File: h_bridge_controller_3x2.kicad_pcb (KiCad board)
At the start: 2 copper layers, 69.8 x 40.6 mm, 1 part

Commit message: Progress towards v1.0.
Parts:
- added C1: 0.1uF, h_bridge_controller_3x2:SM1210, F.Cu at (226.1, 101.3)
- added C2: 0.1uF, h_bridge_controller_3x2:SM1210, F.Cu at (238.4, 91.5)
- added C3: 47uF, h_bridge_controller_3x2:SM2917_POL, F.Cu at (208.5, 105.6)
- added D1: diode_schottky_45V_10A, h_bridge_controller_3x2:CFP15, F.Cu at (175.5, 120.5)
- added D2: diode_schottky_40V_1A, h_bridge_controller_3x2:DO-214AC(SMA), F.Cu at (175.0, 97.2)
- added D3: diode_schottky_40V_1A, h_bridge_controller_3x2:DO-214AC(SMA), F.Cu at (175.0, 103.9)
- added D4: diode_schottky_40V_1A, h_bridge_controller_3x2:DO-214AC(SMA), F.Cu at (209.8, 71.2)
- added D5: diode_schottky_40V_1A, h_bridge_controller_3x2:DO-214AC(SMA), F.Cu at (209.8, 77.9)
- added D6: diode_schottky_40V_1A, h_bridge_controller_3x2:DO-214AC(SMA), F.Cu at (193.1, 97.2)
- added D7: diode_schottky_40V_1A, h_bridge_controller_3x2:DO-214AC(SMA), F.Cu at (193.1, 103.9)
- added D8: diode_schottky_40V_1A, h_bridge_controller_3x2:DO-214AC(SMA), F.Cu at (227.9, 71.2)
- added D9: diode_schottky_40V_1A, h_bridge_controller_3x2:DO-214AC(SMA), F.Cu at (209.8, 84.6)
- added L1: LED_24V, h_bridge_controller_3x2:LED_555-3XXX, F.Cu at (205.8, 95.5)
- added L2: LED_24V, h_bridge_controller_3x2:LED_555-3XXX, F.Cu at (212.8, 95.5)
- added L3: LED_24V, h_bridge_controller_3x2:LED_555-3XXX, F.Cu at (219.9, 98.2)
- added L4: LED_24V, h_bridge_controller_3x2:LED_555-3XXX, F.Cu at (239.3, 82.1)
- added L5: LED_24V, h_bridge_controller_3x2:LED_555-3XXX, F.Cu at (256.4, 75.3)
- added P1: PWR_JACK_2.5x5.5, h_bridge_controller_3x2:DCJACK_2PIN_HIGHCURRENT, F.Cu at (155.6, 88.9)
- added R1: 0.5, h_bridge_controller_3x2:SM2010, F.Cu at (217.0, 107.6)
- added R2: 0.5, h_bridge_controller_3x2:SM2010, F.Cu at (227.1, 94.4)
- added SW1: SPST_SLIDE_AS, h_bridge_controller_3x2:SPST_SLIDE_AS, F.Cu at (170.0, 132.4)
- added T1: TERM_BLK_HDR_2POS_VERT_0.2IN, h_bridge_controller_3x2:TERM_BLK_HDR_2POS_VERT_0.2IN, F.Cu at (192.0, 81.2)
- added T2: TERM_BLK_HDR_2POS_VERT_0.2IN, h_bridge_controller_3x2:TERM_BLK_HDR_2POS_VERT_0.2IN, F.Cu at (174.6, 81.2)
- added U1: L298, h_bridge_controller_3x2:POWERSO20, F.Cu at (227.3, 82.9)
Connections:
- MDB1 pad 14: (no net) -> /SENSE_0
- MDB1 pad 15: (no net) -> /SENSE_1
- MDB1 pad 18: (no net) -> /DIR_A_0
- MDB1 pad 19: (no net) -> /DIR_B_0
- MDB1 pad 20: (no net) -> /DIR_A_1
- MDB1 pad 21: (no net) -> /DIR_B_1
- MDB1 pad 22: (no net) -> /ENABLE_0
- MDB1 pad 23: (no net) -> /ENABLE_1
- MDB1 pad GND: (no net) -> GND
- MDB1 pad VDD: (no net) -> VDD
- MDB1 pad VEE: (no net) -> VEE
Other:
- board text added: "Janelia Modular Device h_bridge_controller part_number: 1171 03/2017 ver 1.0 3x2"
- board text removed: "Janelia Modular Device template part_number: 1000 02/2017 ver 1.0 3x2"

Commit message: Finished version 1.0.
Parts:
- added SW2: SPST_SLIDE_AS, h_bridge_controller_3x2:SPST_SLIDE_AS, F.Cu at (105.4, 92.7)
- added SW3: SPST_SLIDE_AS, h_bridge_controller_3x2:SPST_SLIDE_AS, F.Cu at (129.5, 92.7)
- C1, C2, C3, D1, D2, D3, D4, D5, D6, D7, D8, D9, R1, R2, U1: moved to B.Cu
- moved C1 120.8 mm to (105.4, 94.6), turned to 90 degrees
- moved L5 119.5 mm to (137.2, 83.2)
- moved L4 117.4 mm to (121.9, 83.2)
- moved L2 115.7 mm to (97.8, 83.2)
- moved R1 111.7 mm to (105.4, 101.0), turned to 180 degrees
- moved U1 110.7 mm to (117.5, 96.5), turned to 90 degrees
- moved C3 110.6 mm to (98.4, 94.6), turned to 90 degrees
- moved C2 108.9 mm to (129.5, 94.6), turned to 90 degrees
- moved L3 108.0 mm to (113.0, 83.2)
- moved D5 102.4 mm to (108.0, 88.3), turned to 270 degrees
- moved D4 102.1 mm to (108.0, 78.1), turned to 270 degrees
- moved R2 97.8 mm to (129.5, 101.0)
- moved D8 96.1 mm to (132.1, 78.1), turned to 270 degrees
- moved D1 91.6 mm to (89.5, 88.9)
- moved T1 86.6 mm to (105.4, 83.2), turned to 180 degrees
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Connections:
- MDB1 pad 5: (no net) -> /USER_ENABLE_0
- MDB1 pad 6: (no net) -> /USER_ENABLE_1
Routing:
- net GND: track 0.00 -> 151.2 mm, vias 0 -> 1
- net VAA: track 0.00 -> 109.4 mm
- net /DIR_A_0: track 0.00 -> 108.9 mm
- net LED_GND: track 0.00 -> 78.1 mm
- net VEE: track 0.00 -> 70.3 mm, vias 0 -> 2
- net /USER_ENABLE_1: track 0.00 -> 70.0 mm
- net /ENABLE_1: track 0.00 -> 43.4 mm, vias 0 -> 1
- net /h_bridge_0/OUT_+_0: track 0.00 -> 42.0 mm, vias 0 -> 1
- net /h_bridge_0/OUT_-_1: track 0.00 -> 34.3 mm
- net /h_bridge_0/OUT_-_0: track 0.00 -> 33.4 mm, vias 0 -> 1
- net /h_bridge_0/OUT_+_1: track 0.00 -> 32.2 mm
- net /DIR_A_1: track 0.00 -> 30.1 mm, vias 0 -> 1
- net /USER_ENABLE_0: track 0.00 -> 29.8 mm
- net /DIR_B_0: track 0.00 -> 28.5 mm, vias 0 -> 1
- net /DIR_B_1: track 0.00 -> 28.3 mm, vias 0 -> 1
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- added copper zone on F.Cu, net GND
- added copper zone on B.Cu, net VAA
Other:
- net class GND: trace_width 0.4064 -> 1.2192
- board text added: "+"
- board text added: "+9-42VDC"
- board text added: "-"
- board text added: "0"
- board text added: "1"
- board text added: "2.5x5.5 Center +"
- board text added: "Lights"

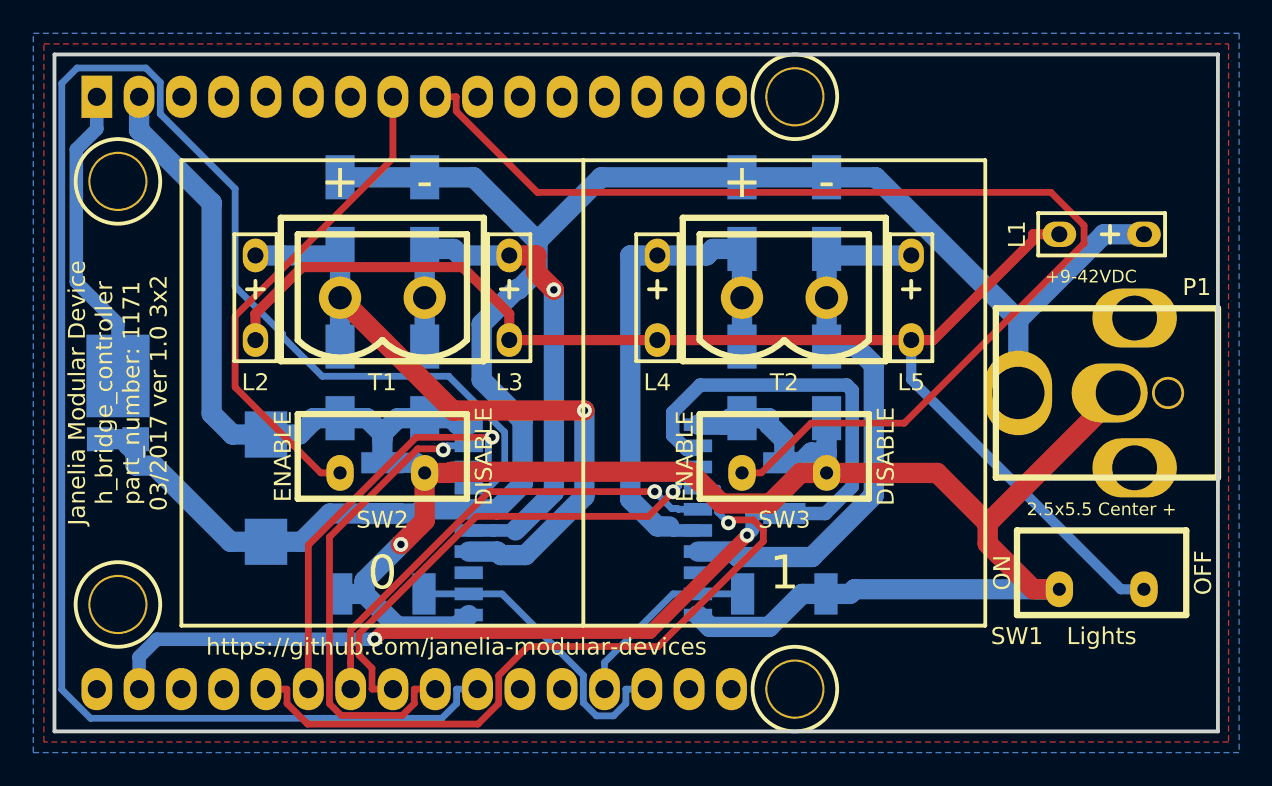
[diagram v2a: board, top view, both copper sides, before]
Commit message: Moved edges.
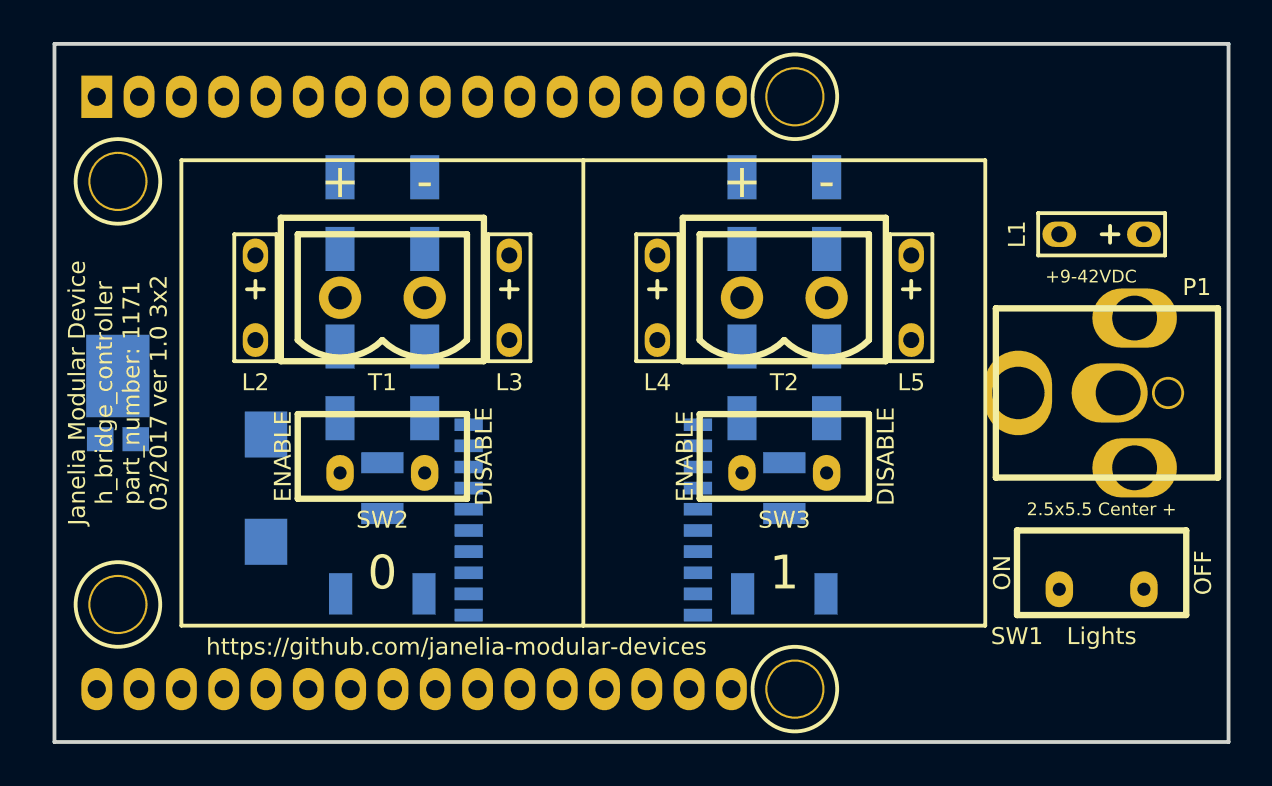
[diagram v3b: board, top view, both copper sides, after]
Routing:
- net GND: track 151.2 -> 0.00 mm, vias 1 -> 0
- net VAA: track 109.4 -> 0.00 mm
- net /DIR_A_0: track 108.9 -> 0.00 mm
- net LED_GND: track 78.1 -> 0.00 mm
- net VEE: track 70.3 -> 0.00 mm, vias 2 -> 0
- net /USER_ENABLE_1: track 70.0 -> 0.00 mm
- net /ENABLE_1: track 43.4 -> 0.00 mm, vias 1 -> 0
- net /h_bridge_0/OUT_+_0: track 42.0 -> 0.00 mm, vias 1 -> 0
- net /h_bridge_0/OUT_-_1: track 34.3 -> 0.00 mm
- net /h_bridge_0/OUT_-_0: track 33.4 -> 0.00 mm, vias 1 -> 0
- net /h_bridge_0/OUT_+_1: track 32.2 -> 0.00 mm
- net /DIR_A_1: track 30.1 -> 0.00 mm, vias 1 -> 0
- net /USER_ENABLE_0: track 29.8 -> 0.00 mm
- net /DIR_B_0: track 28.5 -> 0.00 mm, vias 1 -> 0
- net /DIR_B_1: track 28.3 -> 0.00 mm, vias 1 -> 0
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- removed copper zone on F.Cu, net GND
- removed copper zone on B.Cu, net VAA
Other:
- board size 69.8 x 40.6 mm -> 70.5 x 41.9 mm

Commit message: Renamed (SMA) to _SMA.
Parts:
- D2, D3, D4, D5, D6, D7, D8, D9: footprint h_bridge_controller_3x2:DO-214AC(SMA) -> h_bridge_controller_3x2:DO-214AC_SMA
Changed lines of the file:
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@@
       (net 1 VAA) (solder_mask_margin 0.1) (clearance 0.1))
   )
-  (module "h_bridge_controller_3x2:DO-214AC(SMA)" (layer B.Cu)
+  (module "h_bridge_controller_3x2:DO-214AC_SMA" (layer B.Cu)
     (at 102.87 78.105 270)
     (fp_text reference D2 (at 0 -2.54 270) (layer B.SilkS)
@@
       (net 1 VAA))
   )
-  (module "h_bridge_controller_3x2:DO-214AC(SMA)" (layer B.Cu)
+  (module "h_bridge_controller_3x2:DO-214AC_SMA" (layer B.Cu)
     (at 102.87 88.265 270)
     (fp_text reference D3 (at 0 -2.54 270) (layer B.SilkS)
@@
       (net 2 GND))
   )
-  (module "h_bridge_controller_3x2:DO-214AC(SMA)" (layer B.Cu)
+  (module "h_bridge_controller_3x2:DO-214AC_SMA" (layer B.Cu)
     (at 107.95 78.105 270)
     (fp_text reference D4 (at 0 -2.54 270) (layer B.SilkS)
@@
       (net 1 VAA))
   )
-  (module "h_bridge_controller_3x2:DO-214AC(SMA)" (layer B.Cu)
+  (module "h_bridge_controller_3x2:DO-214AC_SMA" (layer B.Cu)
     (at 107.95 88.265 270)
     (fp_text reference D5 (at 0 -2.54 270) (layer B.SilkS)
@@
       (net 2 GND))
   )
-  (module "h_bridge_controller_3x2:DO-214AC(SMA)" (layer B.Cu)
+  (module "h_bridge_controller_3x2:DO-214AC_SMA" (layer B.Cu)
     (at 127 78.105 270)
     (fp_text reference D6 (at 0 -2.54 270) (layer B.SilkS)
@@
       (net 7 /h_bridge_0/OUT_+_1))
   )
-  (module "h_bridge_controller_3x2:DO-214AC(SMA)" (layer B.Cu)
+  (module "h_bridge_controller_3x2:DO-214AC_SMA" (layer B.Cu)
     (at 127 88.265 270)
     (fp_text reference D7 (at 0 -2.54 270) (layer B.SilkS)
@@
       (net 7 /h_bridge_0/OUT_+_1))
   )
-  (module "h_bridge_controller_3x2:DO-214AC(SMA)" (layer B.Cu)
+  (module "h_bridge_controller_3x2:DO-214AC_SMA" (layer B.Cu)
     (at 132.08 78.105 270)
     (fp_text reference D8 (at 0 -2.54 270) (layer B.SilkS)
@@
       (net 8 /h_bridge_0/OUT_-_1))
   )
-  (module "h_bridge_controller_3x2:DO-214AC(SMA)" (layer B.Cu)
+  (module "h_bridge_controller_3x2:DO-214AC_SMA" (layer B.Cu)
     (at 132.08 88.265 270)
     (fp_text reference D9 (at 0 -2.54 270) (layer B.SilkS)
